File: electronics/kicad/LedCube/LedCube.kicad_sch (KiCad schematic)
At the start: 2 parts

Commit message: Add connectors to KiCad schematic
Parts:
- added J?: COM, Connector_PinHeader_1.27mm:PinHeader_2x03_P1.27mm_Vertical, symbol Connector_Generic:Conn_02x03_Odd_Even
- added J? (x3): Conn_01x03, Connector_JST:JST_XH_B3B-XH-A_1x03_P2.50mm_Vertical, symbol Connector_Generic:Conn_01x03
- added J?: JTAG, Connector_PinHeader_1.27mm:PinHeader_2x05_P1.27mm_Vertical, symbol Connector_Generic:Conn_02x05_Odd_Even
- added J?: USB_C_Receptacle, Connector_USB:USB_C_Receptacle_GCT_USB4105-xx-A_16P_TopMnt_Horizontal, symbol Connector:USB_C_Receptacle_USB2.0
- added J?: Conn_01x02, Connector_JST:JST_XH_B2B-XH-AM_1x02_P2.50mm_Vertical, symbol Connector_Generic:Conn_01x02
- added R? (x9): 220, Resistor_SMD:R_0603_1608Metric_Pad0.98x0.95mm_HandSolder, symbol Device:R_Small
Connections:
- new net: J?.1 (Pin_1), R?.2 (x3)
- new net: J?.2 (Pin_2), R?.2 (x3)
- new net: J?.3 (Pin_3), R?.2 (x3)
- new net: J?.A4 (VBUS), J?.A9 (VBUS), J?.B4 (VBUS), J?.B9 (VBUS)
- new net +3V3: J?.1 (Pin_1), J?.2 (Pin_2)
- new net +5V: J?.1 (Pin_1)
- new net D0: R?.1
- new net D1: R?.1
- new net D2: R?.1
- new net D3: R?.1
- new net D4: R?.1
- new net D5: R?.1
- new net D6: R?.1
- new net D7: R?.1
- new net D8: R?.1
- new net GND: J?.2 (Pin_2), J?.3 (Pin_3), J?.4 (Pin_4), J?.5 (Pin_5), J?.7 (Pin_7), J?.9 (Pin_9), J?.A1 (GND), J?.A12 (GND), J?.B1 (GND), J?.B12 (GND)
- new net GPIO_0: J?.6 (Pin_6)
- new net RESET: J?.1 (Pin_1)
- new net RX: J?.5 (Pin_5)
- new net TCK: J?.4 (Pin_4)
- new net TDI: J?.8 (Pin_8)
- new net TDO: J?.6 (Pin_6)
- new net TMS: J?.2 (Pin_2)
- new net TX: J?.3 (Pin_3)
- no-connect marks 0 -> 8
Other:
- note added: "Led Pin Connectors"
- note added: "Power Connector"
- note added: "Programming Connectors"
- note added: "Screen Connector"
- moved on the sheet: U?

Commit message: Update kicad schematic
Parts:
- removed J?: USB_C_Receptacle, Connector_USB:USB_C_Receptacle_GCT_USB4105-xx-A_16P_TopMnt_Horizontal, symbol Connector:USB_C_Receptacle_USB2.0
- removed U?: ESP32-S3, Package_DFN_QFN:QFN-56-1EP_7x7mm_P0.4mm_EP5.6x5.6mm, symbol Espressif:ESP32-S3
- added C1: 220uF, Capacitor_THT:C_Radial_D6.3mm_H5.0mm_P2.50mm, symbol Device:C_Polarized
- added D1: D, Diode_THT:D_DO-15_P10.16mm_Horizontal, symbol Device:D
- added J4: Conn_01x04, Connectors:Grove_1x04, symbol Connector_Generic:Conn_01x04
- U1: renamed from U?; value ESP32 -> ESP32-DevkitM-1; footprint (none) -> Esp32:ESP32-DevKitC
- gave numbers to parts that had none: 15
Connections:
- net +3V3: now also J4.1 (Pin_1)
- net +5V: now also C1.1, D1.1 (K); no longer J6.1 (Pin_1)
- net GND: now also C1.2, J4.2 (Pin_2)
- net RX renamed UART0_RX
- net TX renamed UART0_TX
- new net: D1.2 (A), J6.1 (Pin_1)
- new net UART1_RX: J4.3 (Pin_3)
- new net UART1_TX: J4.4 (Pin_4)
- no-connect marks 8 -> 1
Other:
- note added: "Display Connector"
- note added: "ESP32-DevkitM-1"
- note added: "Led Data Pin Connectors"
- note removed: "Led Pin Connectors"
- note removed: "Screen Connector"
- moved on the sheet: J1, J2, J3, J5, J6, J7, R1, R2, R3, R4, R5, R6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

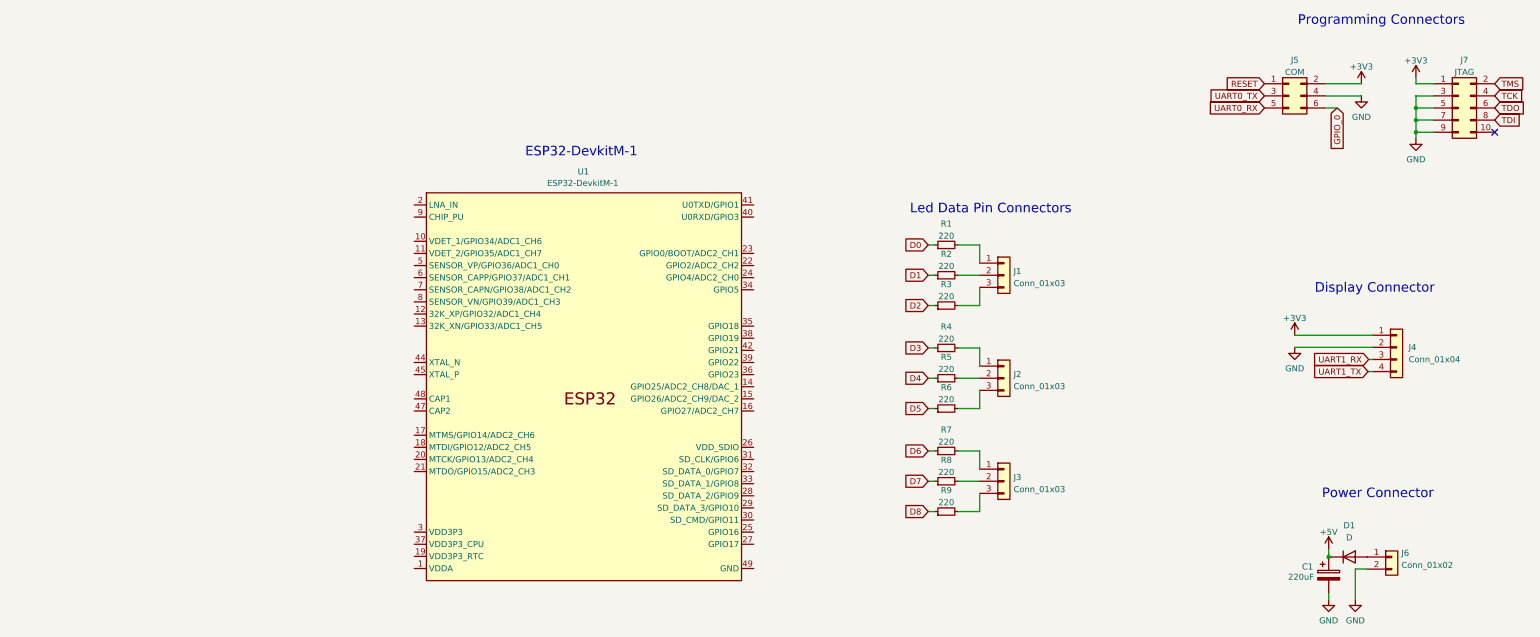
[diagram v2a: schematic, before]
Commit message: Add esp32 devkit footprint
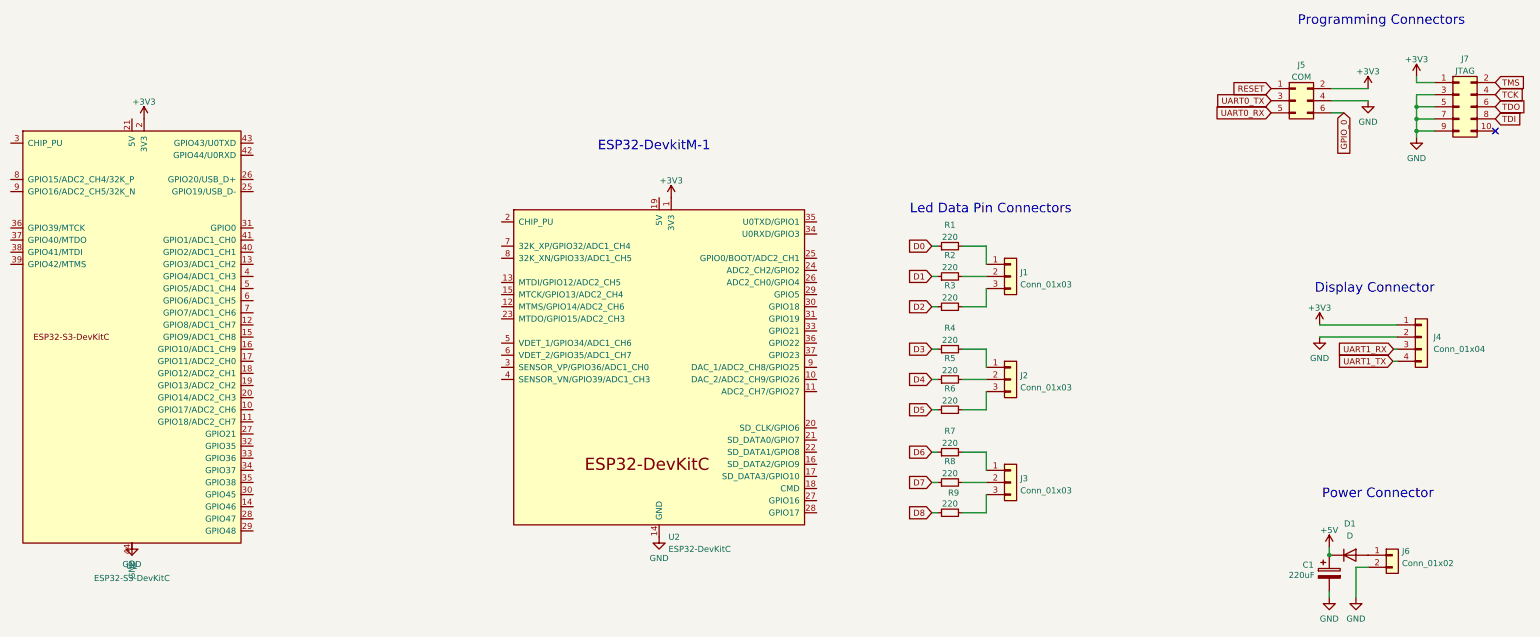
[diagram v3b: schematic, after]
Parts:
- removed U1: ESP32-DevkitM-1, Esp32:ESP32-DevKitC, symbol Espressif:ESP32
- added U1: ESP32-S3-DevKitC, Espressif:ESP32-S3-DevKitC, symbol esp32:ESP32-S3-DevKitC
- added U2: ESP32-DevKitC, Esp32:ESP32-DevKitC, symbol esp32:ESP32-DevKitC
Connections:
- net +3V3: now also U1.1 (3V3), U1.2 (3V3), U2.1 (3V3)
- net GND: now also U1.22 (GND), U1.23 (GND), U1.24 (GND), U1.44 (GND), U2.14 (GND), U2.32 (GND), U2.38 (GND)
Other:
- moved on the sheet: J1, J2, J3, J4, J5, R1, R2, R3, R4, R5, R6, R7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

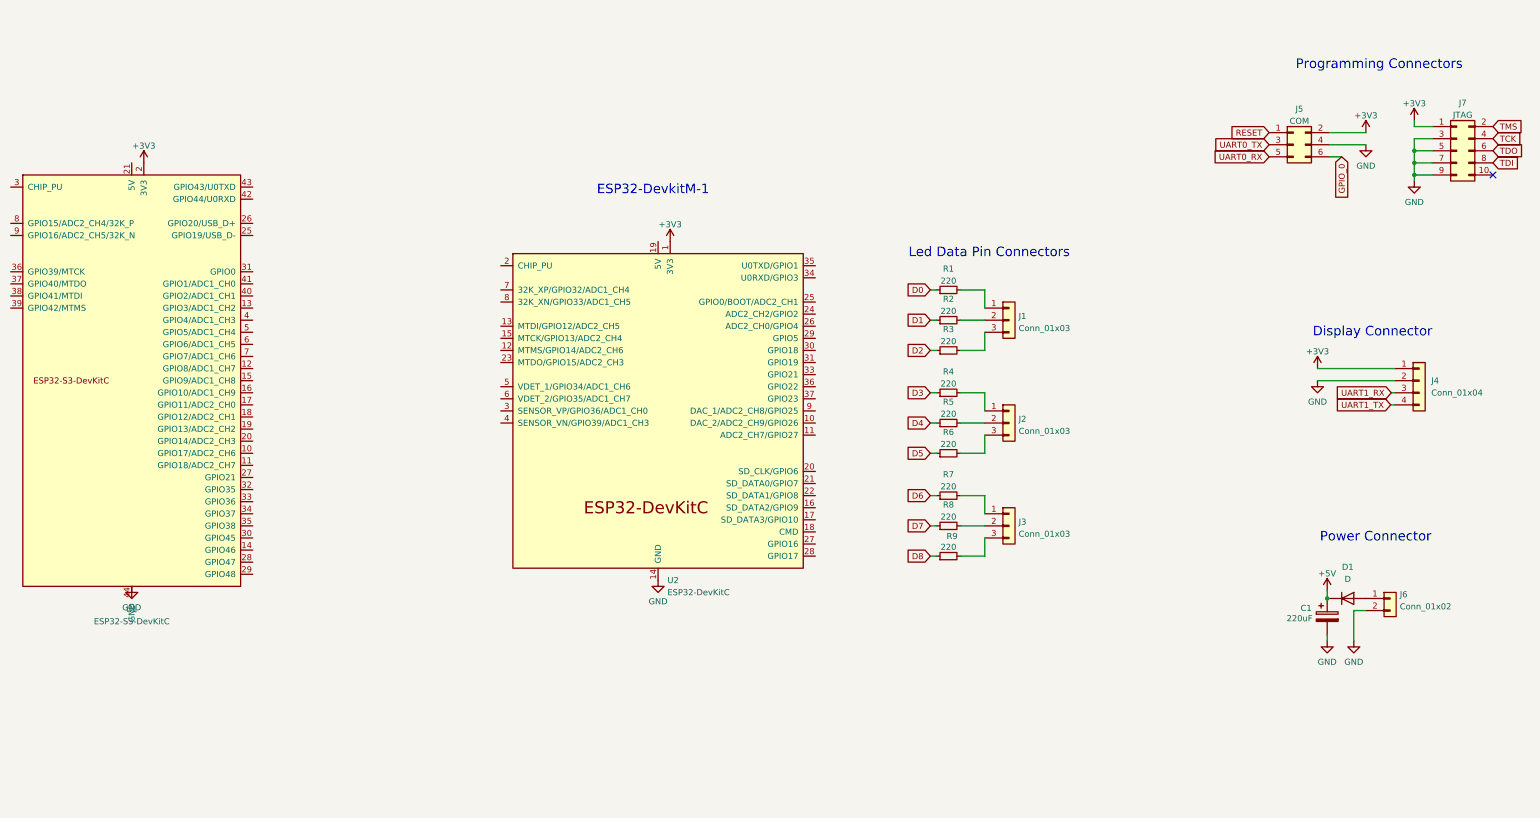
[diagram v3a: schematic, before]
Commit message: Create ESP32-DevkitM-1 footprint
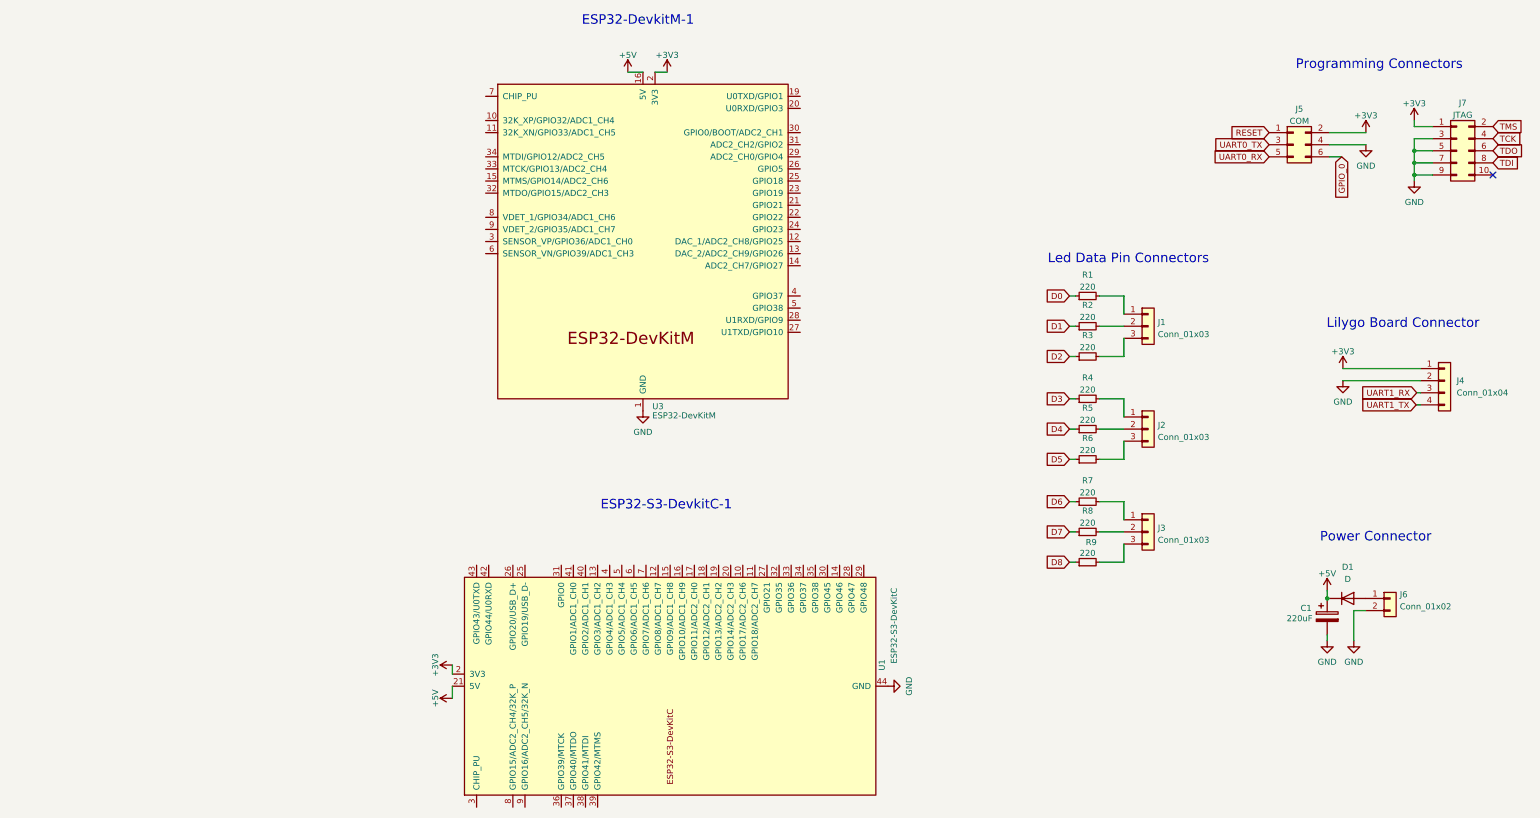
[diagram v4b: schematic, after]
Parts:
- removed U2: ESP32-DevKitC, Esp32:ESP32-DevKitC, symbol esp32:ESP32-DevKitC
- added U3: ESP32-DevKitM, Espressif:ESP32-DevKitC, symbol esp32:ESP32-DevKitM
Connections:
- net +3V3: now also U3.2 (3V3)
- net +5V: now also U1.21 (5V), U3.16 (5V)
- net GND: now also U3.1 (GND), U3.17 (GND), U3.18 (GND)
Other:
- note added: "ESP32-S3-DevkitC-1"
- note added: "Lilygo Board Connector"
- note removed: "Display Connector"
- moved on the sheet: J1, J2, J3, J4, R1, R2, R3, R4, R5, R6, R7, R8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

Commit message: Finish KiCad PCB board
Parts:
- removed U1: ESP32-S3-DevKitC, Espressif:ESP32-S3-DevKitC, symbol esp32:ESP32-S3-DevKitC
- added C2: 100uF, Capacitor_THT:C_Radial_D5.0mm_H5.0mm_P2.00mm, symbol Device:C_Polarized
- added H1, H2, H3, H4: MountingHole, MountingHole:MountingHole_3.2mm_M3_Pad, symbol Mechanical:MountingHole
- C1: value 220uF -> 100uF; footprint Capacitor_THT:C_Radial_D6.3mm_H5.0mm_P2.50mm -> Capacitor_THT:C_Radial_D5.0mm_H5.0mm_P2.00mm
- J5: footprint Connector_PinHeader_1.27mm:PinHeader_2x03_P1.27mm_Vertical -> Connectors:ESP_PROG_COM
- J6: footprint Connector_JST:JST_XH_B2B-XH-AM_1x02_P2.50mm_Vertical -> Connector_JST:JST_XH_B2B-XH-A_1x02_P2.50mm_Vertical
- J7: footprint Connector_PinHeader_1.27mm:PinHeader_2x05_P1.27mm_Vertical -> Connectors:ESP_PROG_JTAG
- U3: footprint Espressif:ESP32-DevKitC -> Espressif:ESP32-DevKitM
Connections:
- net +3V3: now also C2.1
- net D0: now also U3.22 (GPIO22)
- net D1: now also U3.23 (GPIO19)
- net D2: now also U3.24 (GPIO23)
- net D3: now also U3.25 (GPIO18)
- net D4: now also U3.10 (32K_XP/GPIO32/ADC1_CH4)
- net D5: now also U3.11 (32K_XN/GPIO33/ADC1_CH5)
- net D6: now also U3.12 (DAC_1/ADC2_CH8/GPIO25)
- net D7: now also U3.13 (DAC_2/ADC2_CH9/GPIO26)
- net D8: now also U3.14 (ADC2_CH7/GPIO27)
- net GND: now also C2.2
- net GPIO_0: now also U3.30 (GPIO0/BOOT/ADC2_CH1)
- net RESET: now also U3.7 (CHIP_PU)
- net TCK: now also U3.33 (MTCK/GPIO13/ADC2_CH4)
- net TDI: now also U3.34 (MTDI/GPIO12/ADC2_CH5)
- net TDO: now also U3.32 (MTDO/GPIO15/ADC2_CH3)
- net TMS: now also U3.15 (MTMS/GPIO14/ADC2_CH6)
- net UART0_RX: now also U3.20 (U0RXD/GPIO3)
- net UART0_TX: now also U3.19 (U0TXD/GPIO1)
- net UART1_RX: now also U3.28 (U1RXD/GPIO9)
- net UART1_TX: now also U3.27 (U1TXD/GPIO10)
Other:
- note added: "Connector"
- note added: "MCU"
- note added: "Mounting"
- note added: "Programing"
- note removed: "ESP32-S3-DevkitC-1"
- title: (none) -> Led Cube Board
- moved on the sheet: C1, D1, J1, J2, J3, J4, J5, J6, J7, R1, R2, R3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

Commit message: Update kicad gerbers
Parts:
- D1: value D -> 1N4002
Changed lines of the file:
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@@
   )
   (symbol (lib_id "Device:D") (at 236.22 138.43 0) (unit 1)
-    (in_bom yes) (on_board yes) (dnp no) (fields_autoplaced)
-    (property "Reference" "D1" (at 236.22 131.826 0)
+    (in_bom yes) (on_board yes) (dnp no)
+    (property "Reference" "D1" (at 236.22 134.1501 0)
       (effects (font (size 1.27 1.27)))
     )
-    (property "Value" "D" (at 236.22 134.366 0)
+    (property "Value" "1N4002" (at 236.855 135.89 0)
       (effects (font (size 1.27 1.27)))
     )
